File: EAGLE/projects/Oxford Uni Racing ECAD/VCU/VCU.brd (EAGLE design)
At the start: 160 x 100 mm, 0 parts

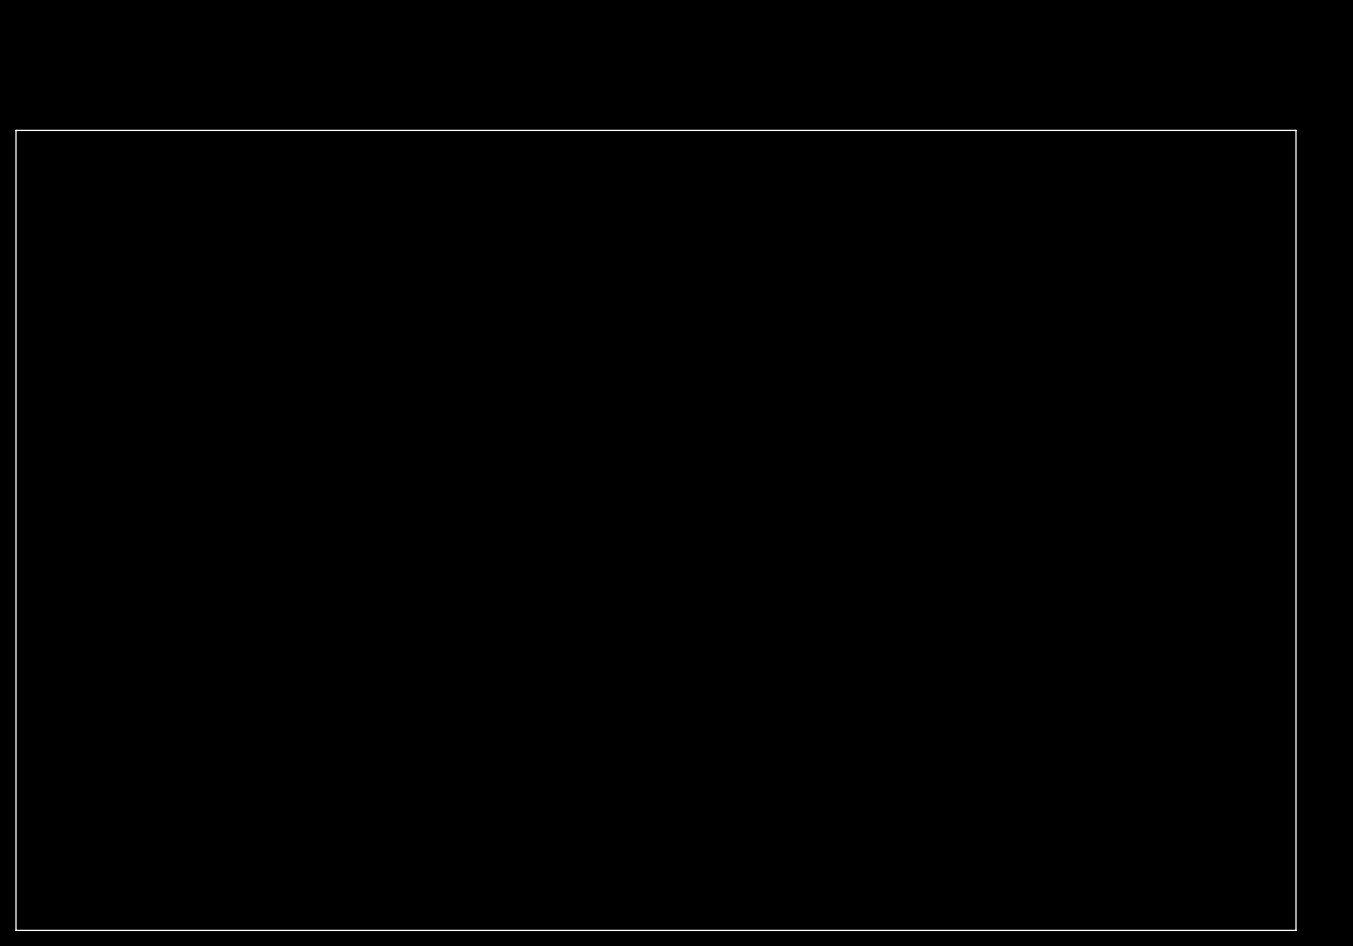
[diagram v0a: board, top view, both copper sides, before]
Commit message: added CAN connector to VCU
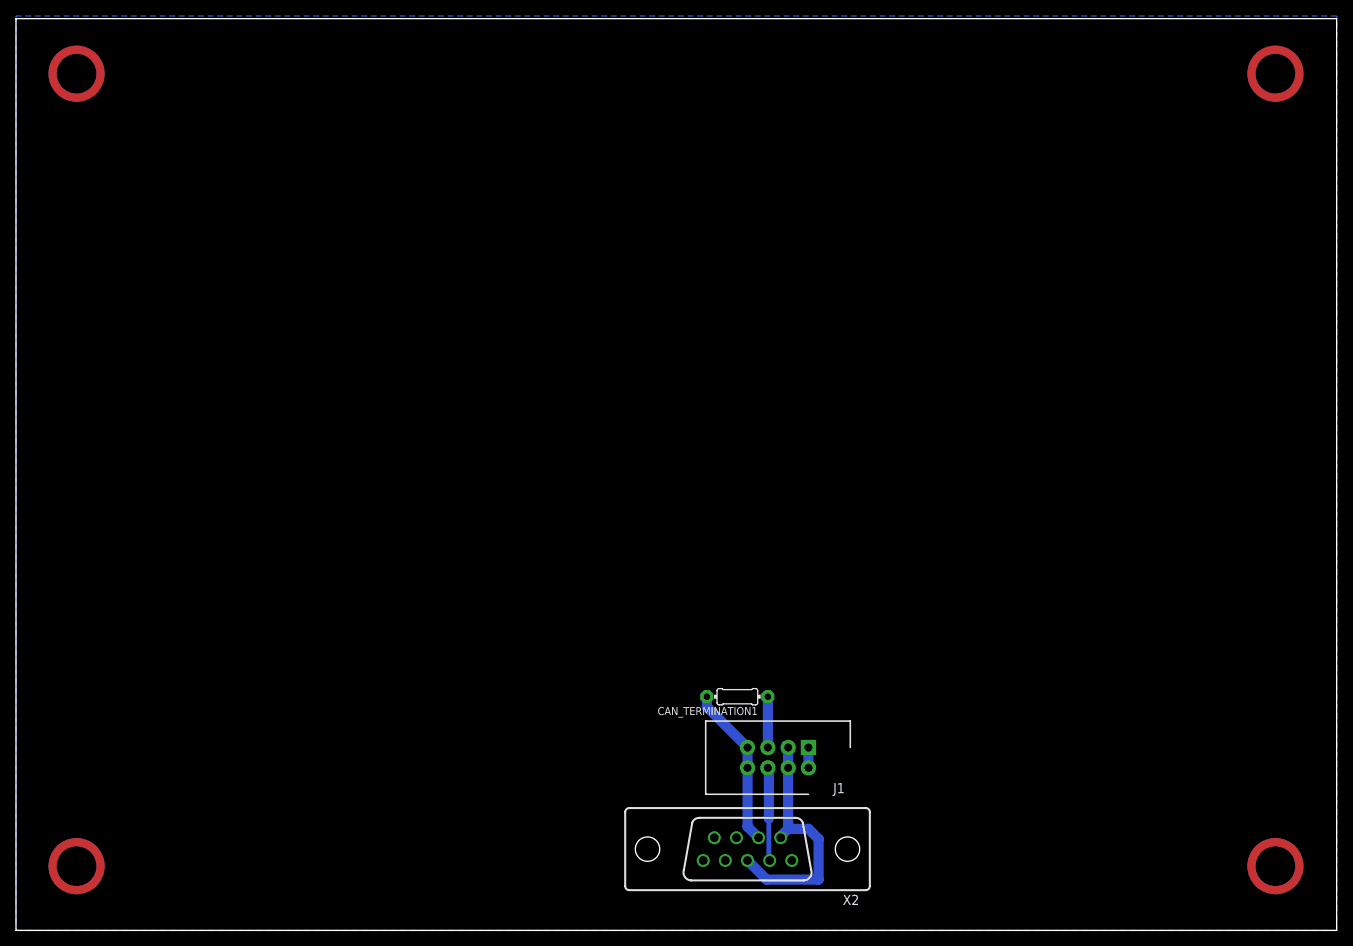
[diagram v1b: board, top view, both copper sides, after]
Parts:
- added CAN_TERMINATION1: 120, adafruit:0204/7
- added J1: T821108A1S100CEU, T821108A1S100CEU:HDRV8W64P254_2X4_1778X895X915P
- added X2: D-SUB9-H2M09ST, con-thomas-betts:H2M09ST
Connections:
- new net 12V: J1.1, J1.2
- new net 5V: X2.9
- new net CANH: CAN_TERMINATION1.2, J1.7, J1.8, X2.7
- new net CANL: CAN_TERMINATION1.1, J1.5, J1.6, X2.2
- new net GND: J1.3, J1.4, X2.3, X2.6
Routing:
- net GND: track 0.00 -> 31.0 mm
- net CANH: track 0.00 -> 20.3 mm
- net CANL: track 0.00 -> 18.9 mm
- net 12V: track 0.00 -> 2.54 mm
- added copper zone on layer 16, net GND
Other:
- board size 160 x 100 mm -> 165.1 x 114 mm
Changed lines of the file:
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@@
 <layer number="230" name="230bmp" color="7" fill="1" visible="yes" active="yes"/>
 <layer number="231" name="231bmp" color="7" fill="1" visible="yes" active="yes"/>
+<layer number="232" name="Eagle3D_PG2" color="7" fill="1" visible="yes" active="yes"/>
+<layer number="233" name="Eagle3D_PG3" color="7" fill="1" visible="yes" active="yes"/>
 <layer number="248" name="Housing" color="7" fill="1" visible="yes" active="yes"/>
 <layer number="249" name="Edge" color="7" fill="1" visible="yes" active="yes"/>
@@
 <board>
 <plain>
-<wire x1="0" y1="0" x2="160" y2="0" width="0" layer="20"/>
-<wire x1="160" y1="0" x2="160" y2="100" width="0" layer="20"/>
-<wire x1="160" y1="100" x2="0" y2="100" width="0" layer="20"/>
-<wire x1="0" y1="100" x2="0" y2="0" width="0" layer="20"/>
+<wire x1="0" y1="0" x2="165.08" y2="0" width="0" layer="20"/>
+<wire x1="165.08" y1="0" x2="165.08" y2="113.97" width="0" layer="20"/>
+<wire x1="165.08" y1="113.97" x2="0" y2="113.97" width="0" layer="20"/>
+<wire x1="0" y1="113.97" x2="0" y2="0" width="0" layer="20"/>
+<wire x1="0" y1="0" x2="165.1" y2="0" width="0.1524" layer="49"/>
+<wire x1="165.1" y1="0" x2="165.1" y2="114.3" width="0.1524" layer="49"/>
+<wire x1="165.1" y1="114.3" x2="0" y2="114.3" width="0.1524" layer="49"/>
+<wire x1="0" y1="114.3" x2="0" y2="0" width="0.1524" layer="49"/>
+<circle x="7.57" y="107.09" locked="yes" radius="3" width="1.016" layer="16"/>
+<circle x="157.43" y="107.09" locked="yes" radius="3" width="1.016" layer="16"/>
+<circle x="7.57" y="8.03" locked="yes" radius="3" width="1.016" layer="16"/>
+<circle x="157.43" y="8.03" locked="yes" radius="3" width="1.016" layer="16"/>
+<circle x="7.57" y="107.09" locked="yes" radius="3" width="1.016" layer="1"/>
+<circle x="157.43" y="107.09" locked="yes" radius="3" width="1.016" layer="1"/>
+<circle x="157.43" y="8.03" locked="yes" radius="3" width="1.016" layer="1"/>
+<circle x="7.57" y="8.03" locked="yes" radius="3" width="1.016" layer="1"/>
 </plain>
 <attributes>
@@
 </autorouter>
 <elements>
+<element name="X2" library="con-thomas-betts" library_urn="urn:adsk.eagle:library:191" package="H2M09ST" package3d_urn="urn:adsk.eagle:package:10567/1" value="D-SUB9-H2M09ST" x="91.44" y="10.16" smashed="yes" rot="R180">
+<attribute name="MF" value="" x="91.44" y="10.16" size="1.778" layer="27" rot="R180" display="off"/>
+<attribute name="MPN" value="" x="91.44" y="10.16" size="1.778" layer="27" rot="R180" display="off"/>
+<attribute name="NAME" x="105.41" y="4.445" size="1.27" layer="25" rot="R180"/>
+<attribute name="OC_FARNELL" value="unknown" x="91.44" y="10.16" size="1.778" layer="27" rot="R180" display="off"/>
+<attribute name="OC_NEWARK" value="unknown" x="91.44" y="10.16" size="1.778" layer="27" rot="R180" display="off"/>
+<attribute name="VALUE" x="97.155" y="4.445" size="1.27" layer="27" rot="R180"/>
+</element>
+<element name="CAN_TERMINATION1" library="adafruit" library_urn="urn:adsk.eagle:library:420" package="0204/7" package3d_urn="urn:adsk.eagle:package:6240596/1" value="120" x="90.17" y="29.21" smashed="yes" rot="R180">
+<attribute name="NAME" x="92.71" y="27.9146" size="0.9906" layer="25" ratio="12" rot="R180"/>
+<attribute name="VALUE" x="91.7956" y="29.6926" size="0.9906" layer="27" ratio="12" rot="R180"/>
+</element>
+<element name="J1" library="T821108A1S100CEU" package="HDRV8W64P254_2X4_1778X895X915P" value="T821108A1S100CEU" x="99.06" y="22.86" smashed="yes" rot="R180">
+<attribute name="DESCRIPTION" value="HEADER, VERTICAL, 2.54MM, 8WAY Amphenol T821 Series, 2.54mm Pitch 8 Way 2 Row Straight PCB Header, Solder Termination, 3A" x="102.87" y="22.86" size="1.778" layer="27" rot="R180" display="off"/>
+<attribute name="HEIGHT" value="9.15mm" x="102.87" y="22.86" size="1.778" layer="27" rot="R180" display="off"/>
+<attribute name="MANUFACTURER_NAME" value="Amphenol" x="102.87" y="22.86" size="1.778" layer="27" rot="R180" display="off"/>
+<attribute name="MANUFACTURER_PART_NUMBER" value="T821108A1S100CEU" x="102.87" y="22.86" size="1.778" layer="27" rot="R180" display="off"/>
+<attribute name="NAME" x="102.87" y="17.78" size="1.27" layer="25" rot="R180" align="center"/>
+<attribute name="RS_PART_NUMBER" value="1702738" x="102.87" y="22.86" size="1.778" layer="27" rot="R180" display="off"/>
+<attribute name="VALUE" x="99.06" y="25.4" size="1.27" layer="27" rot="R180" align="center"/>
+</element>
 </elements>
 <signals>
+<signal name="GND">
+<polygon width="0.1524" layer="16" isolate="0.3048" locked="yes">
+<vertex x="0" y="114.3"/>
+<vertex x="0" y="0"/>
+<vertex x="165.1" y="0"/>
+<vertex x="165.1" y="114.3"/>
+</polygon>
+<contactref element="X2" pad="3"/>
+<contactref element="X2" pad="6"/>
+<wire x1="96.52" y1="12.7" x2="95.5929" y2="11.7729" width="1.27" layer="16"/>
+<wire x1="95.5929" y1="11.7729" x2="95.5929" y2="11.5824" width="1.27" layer="16"/>
+<wire x1="96.52" y1="12.7" x2="99.06" y2="12.7" width="1.27" layer="16"/>
+<wire x1="99.06" y1="12.7" x2="100.33" y2="11.43" width="1.27" layer="16"/>
+<wire x1="100.33" y1="11.43" x2="100.33" y2="6.35" width="1.27" layer="16"/>
+<wire x1="100.33" y1="6.35" x2="93.8276" y2="6.35" width="1.27" layer="16"/>
+<wire x1="93.8276" y1="6.35" x2="91.44" y2="8.7376" width="1.27" layer="16"/>
+<contactref element="J1" pad="3"/>
+<contactref element="J1" pad="4"/>
+<wire x1="96.52" y1="12.7" x2="96.52" y2="20.32" width="1.27" layer="16"/>
+<wire x1="96.52" y1="20.32" x2="96.52" y2="22.86" width="1.27" layer="16"/>
+</signal>
+<signal name="CANL">
+<contactref element="X2" pad="2"/>
+<wire x1="93.98" y1="14.7717375" x2="94.10065" y2="14.6510875" width="0.6096" layer="16"/>
+<wire x1="94.10065" y1="14.6510875" x2="94.10065" y2="13.97" width="0.6096" layer="16"/>
+<contactref element="CAN_TERMINATION1" pad="1"/>
+<contactref element="J1" pad="5"/>
+<contactref element="J1" pad="6"/>
+<wire x1="93.98" y1="29.21" x2="93.98" y2="22.86" width="1.27" layer="16"/>
+<wire x1="93.98" y1="20.32" x2="94.10065" y2="20.19935" width="1.27" layer="16"/>
+<wire x1="94.10065" y1="20.19935" x2="94.10065" y2="13.97" width="1.27" layer="16"/>
+<wire x1="94.2086" y1="8.7376" x2="94.10065" y2="8.84555" width="0.6096" layer="16"/>
+<wire x1="94.10065" y1="8.84555" x2="94.10065" y2="13.97" width="0.6096" layer="16"/>
+<wire x1="93.98" y1="20.32" x2="93.98" y2="22.86" width="0" layer="19" extent="1-1"/>
+</signal>
+<signal name="CANH">
+<contactref element="X2" pad="7"/>
+<wire x1="92.8243" y1="11.5824" x2="91.44" y2="12.9667" width="1.27" layer="16"/>
+<contactref element="CAN_TERMINATION1" pad="2"/>
+<contactref element="J1" pad="7"/>
+<contactref element="J1" pad="8"/>
+<wire x1="91.44" y1="12.9667" x2="91.44" y2="20.32" width="1.27" layer="16"/>
+<wire x1="91.44" y1="20.32" x2="91.44" y2="22.86" width="1.27" layer="16"/>
+<wire x1="91.44" y1="22.86" x2="86.36" y2="27.94" width="1.27" layer="16"/>
+<wire x1="86.36" y1="27.94" x2="86.36" y2="29.21" width="1.27" layer="16"/>
+</signal>
+<signal name="5V">
+<contactref element="X2" pad="9"/>
+</signal>
+<signal name="12V">
+<contactref element="J1" pad="1"/>
+<contactref element="J1" pad="2"/>
+<wire x1="99.06" y1="20.32" x2="99.06" y2="22.86" width="1.27" layer="16"/>
+</signal>
 </signals>
 <mfgpreviewcolors>
@@
 </board>
 </drawing>
+<compatibility>
+<note version="8.2" severity="warning">
+Since Version 8.2, EAGLE supports online libraries. The ids
+of those online libraries will not be understood (or retained)
+with this version.
+</note>
+<note version="8.3" severity="warning">
+Since Version 8.3, EAGLE supports URNs for individual library
+assets (packages, symbols, and devices). The URNs of those assets
+will not be understood (or retained) with this version.
+</note>
+<note version="8.3" severity="warning">
+Since Version 8.3, EAGLE supports the association of 3D packages
+with devices in libraries, schematics, and board files. Those 3D
+packages will not be understood (or retained) with this version.
+</note>
+<note version="8.5" severity="warning">
+Since Version 8.5, EAGLE supports locking for holes, vias, wires and polygons.
+The locking property on all objects of these types will not be understood in this version.
+</note>
+</compatibility>
 </eagle>
